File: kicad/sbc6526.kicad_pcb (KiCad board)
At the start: 4 copper layers, 100 x 100 mm, 61 parts, among them P1 2k, P2 5k, SW1 UP, SW2 DOWN, SW3 OK, SW4 CANCEL, SW5 RESET, U1 6526, U10 74AC138, U11 74ACT245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

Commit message: Fixed Freq. Meter footprint
Frequency meter footprint was wrong. Top row was reversed.

Minor additions to bootstrap and firmware.
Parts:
- moved R8 14.7 mm to (119.2, 127.9), turned to 180 degrees
- moved R7 9.73 mm to (107.0, 128.0), turned to 0 degrees
- moved R5 0.58 mm to (111.6, 128.0), turned to 180 degrees
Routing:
- net Net-(PIC1-Pad13): track 58.7 -> 20.0 mm
- net /clockmeter/C1: track 7.94 -> 25.5 mm
- net Net-(PIC1-Pad12): track 21.6 -> 35.2 mm
- net /clockmeter/C3: track 29.0 -> 21.8 mm
- net Net-(PIC1-Pad10): track 49.0 -> 55.8 mm
- net /clockmeter/C2: track 16.6 -> 18.7 mm
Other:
- board text added: "sbc6526 v2.0.1"
- board text removed: "sbc6526 v2.0.0"

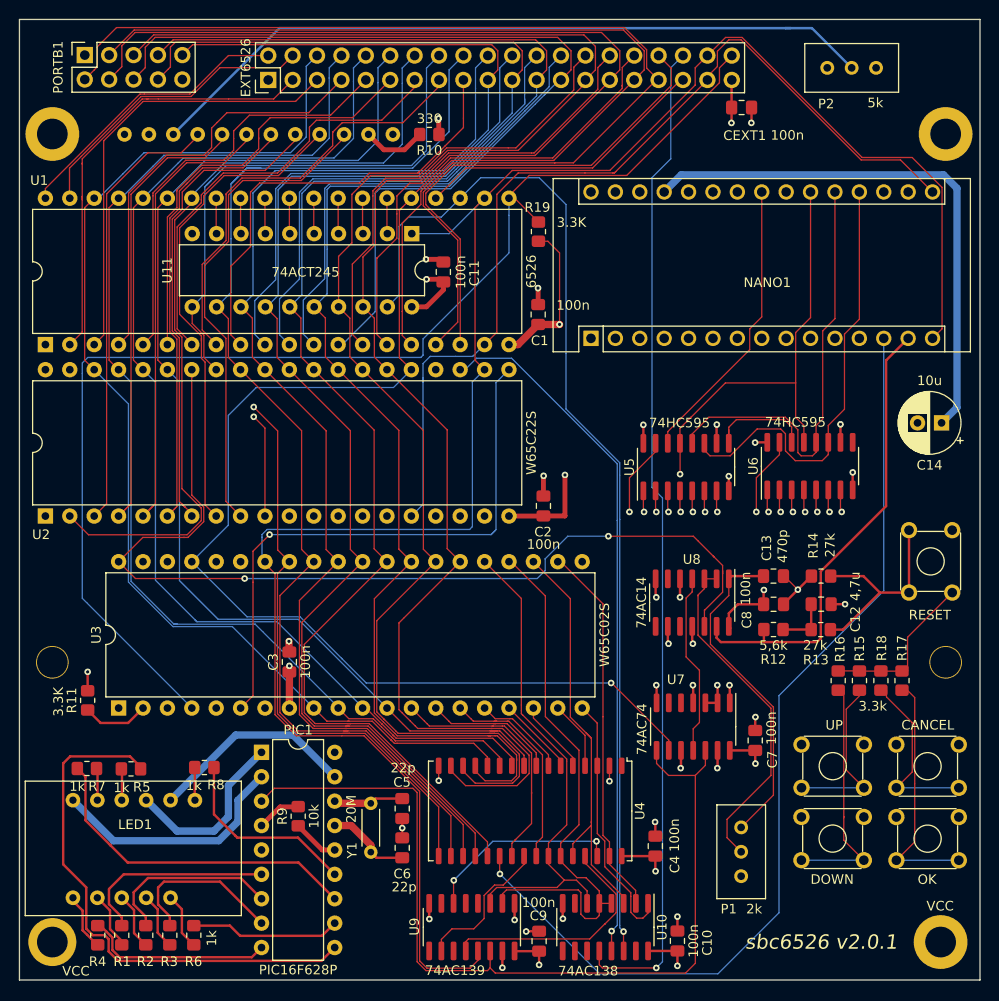
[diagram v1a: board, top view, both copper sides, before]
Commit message: Fixes
* Minor fixes to routing
* Right VCC hole was slightly offset. Fixed
* Removed /CE from arduino to RAM. As RAMCE pulses with PHI, it's not necessary, and we leave /CE tied to GND.
* Fixed RAM footprint, as it was too wide. Improved routing.
* Added current limiting resistor to LCD Contrast
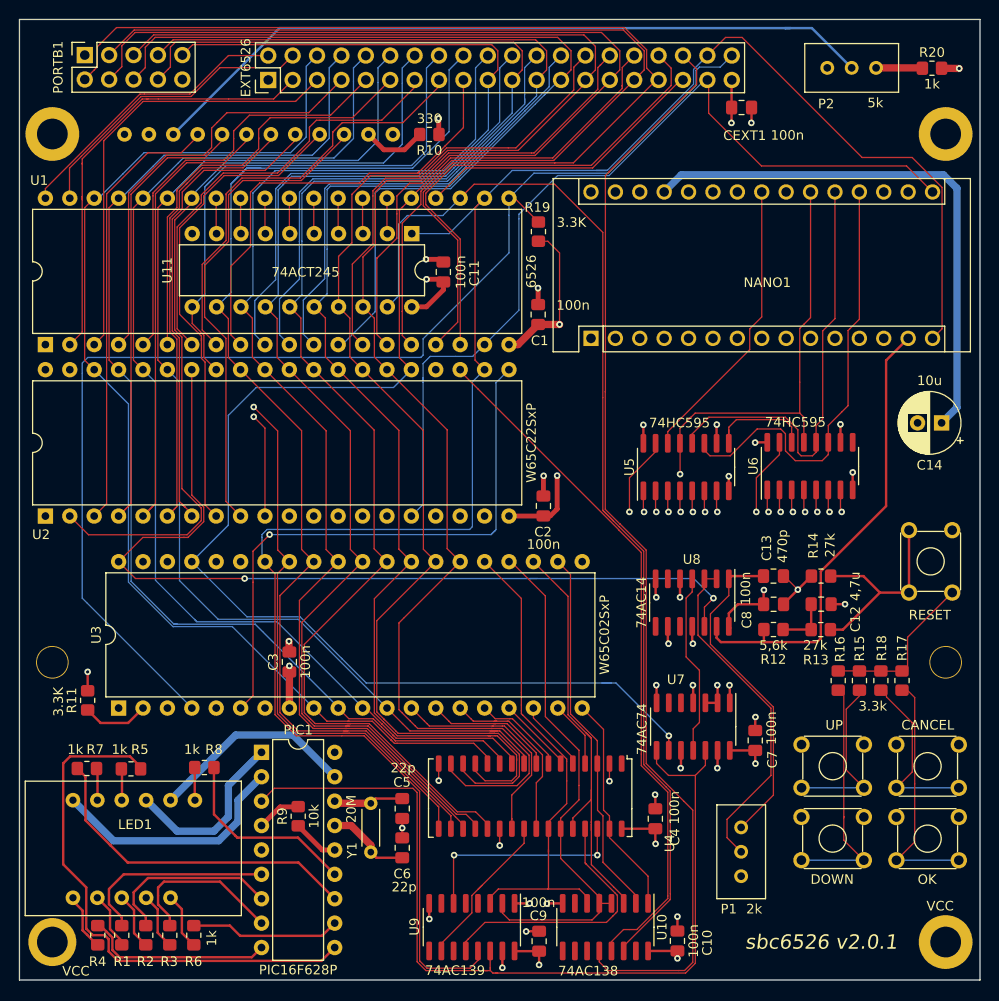
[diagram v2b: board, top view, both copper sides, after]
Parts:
- added R20: 1k, Resistor_SMD:R_0805_2012Metric_Pad1.20x1.40mm_HandSolder, F.Cu at (195.0, 55.1)
- U2: value W65C22S -> W65C22SxP
- U3: value W65C02S -> W65C02SxP
- moved U4 4.56 mm to (155.0, 135.8)
- moved C4 2.85 mm to (166.2, 133.2)
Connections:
- LCD1 pad : GND -> (no net)
- NANO1 pad 13: /~CE -> no_connect_119
- NANO1 pad 17: no_connect_119 -> no_connect_120
- NANO1 pad 18: no_connect_120 -> no_connect_121
- NANO1 pad 2: no_connect_121 -> no_connect_122
- NANO1 pad 22: no_connect_122 -> no_connect_123
- NANO1 pad 24: no_connect_123 -> no_connect_124
- NANO1 pad 25: no_connect_124 -> no_connect_125
- NANO1 pad 28: no_connect_125 -> no_connect_126
- NANO1 pad 3: no_connect_126 -> no_connect_127
- NANO1 pad 30: no_connect_127 -> no_connect_128
- P1 pad 3: no_connect_128 -> no_connect_129
- P2 pad 1: GND -> Net-(P2-Pad1)
- PIC1 pad 18: no_connect_129 -> no_connect_130
- U10 pad 10: no_connect_130 -> no_connect_131
- U10 pad 11: no_connect_131 -> no_connect_132
- U10 pad 15: no_connect_132 -> no_connect_133
- U10 pad 7: no_connect_133 -> no_connect_134
- U10 pad 9: no_connect_134 -> no_connect_135
- U2 pad 15: no_connect_135 -> no_connect_136
- U2 pad 17: no_connect_136 -> no_connect_137
- U2 pad 18: no_connect_137 -> no_connect_138
- U2 pad 19: no_connect_138 -> no_connect_139
- U2 pad 39: no_connect_139 -> no_connect_140
- U2 pad 40: no_connect_140 -> no_connect_141
- U3 pad 1: no_connect_141 -> no_connect_142
- U3 pad 3: no_connect_142 -> no_connect_143
- U3 pad 39: no_connect_143 -> no_connect_144
- U3 pad 5: no_connect_144 -> no_connect_145
- U3 pad 7: no_connect_145 -> no_connect_146
- U4 pad 1: no_connect_146 -> no_connect_147
- U4 pad 22: /~CE -> GND
- U4 pad 3: /A11 -> /A12
- U4 pad 31: /A12 -> /A11
- U6 pad 9: no_connect_147 -> no_connect_148
- U7 pad 5: no_connect_148 -> no_connect_149
- U7 pad 6: no_connect_149 -> no_connect_150
- U8 pad 10: no_connect_150 -> no_connect_151
- U8 pad 6: no_connect_151 -> no_connect_152
- U8 pad 8: no_connect_152 -> no_connect_153
- U9 pad 11: no_connect_153 -> no_connect_154
- U9 pad 4: no_connect_154 -> no_connect_155
- U9 pad 5: no_connect_155 -> no_connect_156
- U9 pad 7: no_connect_156 -> no_connect_157
- U9 pad 9: no_connect_157 -> no_connect_158
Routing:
- net /~CE: track 102.2 -> 0.00 mm, vias 1 -> 0
- net /~CIAEXT: track 104.6 -> 114.3 mm, vias 1 -> 0
- net /~RES: track 102.1 -> 94.6 mm
- net /~CIA: track 109.7 -> 115.4 mm, vias 1 -> 0
- net /TOD: track 100.0 -> 95.1 mm
- net Net-(P2-Pad1): track 0.00 -> 4.84 mm
- net GND: track 48.3 -> 52.0 mm, vias 25 -> 27
- net /A11: track 65.1 -> 61.7 mm
- net /A4: track 65.3 -> 62.2 mm
- net /memory/~WE: track 25.2 -> 28.2 mm
- net /A6: track 57.8 -> 55.0 mm
- net /D1: track 191.6 -> 188.8 mm
- net /D0: track 188.6 -> 185.8 mm
- net /D2: track 181.6 -> 179.4 mm
- net /D3: track 177.0 -> 174.8 mm
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
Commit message: Uploaded firmware v2.0.2
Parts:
- moved R10 1.08 mm to (143.8, 62.0)
- moved U7 0.10 mm to (170.0, 123.6)
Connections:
- net /R~W renamed /R~{W}
- net /memory/~OE renamed /memory/~{OE}
- net /memory/~WE renamed /memory/~{WE}
- net /peripherals/~CIARES renamed /peripherals/~{CIARES}
- net /peripherals/~EXTFLAG renamed /peripherals/~{EXTFLAG}
- net /peripherals/~EXTPC renamed /peripherals/~{EXTPC}
- net /~CIA renamed /~{CIA}
- net /~CIAEXT renamed /~{CIAEXT}
- net /~IRQ renamed /~{IRQ}
- net /~PHI2 renamed /~{PHI2}
- net /~RES renamed /~{RES}
- net /~VIA renamed /~{VIA}
- net /~VIAIRQ renamed /~{VIAIRQ}
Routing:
- net Net-(LCD1-Pad15): track 6.67 -> 7.73 mm
- net /peripherals/PA7: track 47.8 -> 48.6 mm
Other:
- board text added: "sbc6526 v2.0.2"
- board text removed: "sbc6526 v2.0.1"

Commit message: PullUps con SERCLOCK and SERDAT
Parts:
- added R21: 3k3, Resistor_SMD:R_0805_2012Metric_Pad1.20x1.40mm_HandSolder, F.Cu at (102.7, 72.3)
- added R22: 3k3, Resistor_SMD:R_0805_2012Metric_Pad1.20x1.40mm_HandSolder, F.Cu at (105.2, 72.3)
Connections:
- net /BE renamed /bootstrap/BE
- net /PB0 renamed /io/PB0
- net /PB1 renamed /io/PB1
- net /PB2 renamed /io/PB2
- net /PB3 renamed /io/PB3
- net /PB4 renamed /io/PB4
- net /PB5 renamed /io/PB5
- net /PB6 renamed /io/PB6
- net /PB7 renamed /io/PB7
- net /RESET renamed /bootstrap/RESET
- net /VPB1 renamed /peripherals/VPB1
- net /VPB2 renamed /peripherals/VPB2
- net /VPB3 renamed /peripherals/VPB3
- net /VPB4 renamed /peripherals/VPB4
- net /~{CIAEXT} renamed /memory/~{CIAEXT}
- net /~{CIA} renamed /memory/~{CIA}
- net /~{PHI2} renamed /clock/~{PHI2}
- net /~{VIA} renamed /memory/~{VIA}
- LCD1 pad : (no net) -> GND
- NANO1 pad 1: no_connect_118 -> unconnected-(NANO1-Pad1)
- NANO1 pad 13: no_connect_119 -> unconnected-(NANO1-Pad13)
- NANO1 pad 17: no_connect_120 -> unconnected-(NANO1-Pad17)
- NANO1 pad 18: no_connect_121 -> unconnected-(NANO1-Pad18)
- NANO1 pad 2: no_connect_122 -> unconnected-(NANO1-Pad2)
- NANO1 pad 22: no_connect_123 -> unconnected-(NANO1-Pad22)
- NANO1 pad 24: no_connect_124 -> unconnected-(NANO1-Pad24)
- NANO1 pad 25: no_connect_125 -> unconnected-(NANO1-Pad25)
- NANO1 pad 28: no_connect_126 -> unconnected-(NANO1-Pad28)
- NANO1 pad 3: no_connect_127 -> unconnected-(NANO1-Pad3)
- NANO1 pad 30: no_connect_128 -> unconnected-(NANO1-Pad30)
- P1 pad 3: no_connect_129 -> unconnected-(P1-Pad3)
- PIC1 pad 18: no_connect_130 -> unconnected-(PIC1-Pad18)
- U10 pad 10: no_connect_131 -> unconnected-(U10-Pad10)
- U10 pad 11: no_connect_132 -> unconnected-(U10-Pad11)
- U10 pad 15: no_connect_133 -> unconnected-(U10-Pad15)
- U10 pad 7: no_connect_134 -> unconnected-(U10-Pad7)
- U10 pad 9: no_connect_135 -> unconnected-(U10-Pad9)
- U2 pad 15: no_connect_136 -> unconnected-(U2-Pad15)
- U2 pad 17: no_connect_137 -> unconnected-(U2-Pad17)
- U2 pad 18: no_connect_138 -> unconnected-(U2-Pad18)
- U2 pad 19: no_connect_139 -> unconnected-(U2-Pad19)
- U2 pad 39: no_connect_140 -> unconnected-(U2-Pad39)
- U2 pad 40: no_connect_141 -> unconnected-(U2-Pad40)
- U3 pad 1: no_connect_142 -> unconnected-(U3-Pad1)
- U3 pad 3: no_connect_143 -> unconnected-(U3-Pad3)
- U3 pad 35: (no net) -> unconnected-(U3-Pad35)
- U3 pad 39: no_connect_144 -> unconnected-(U3-Pad39)
- U3 pad 5: no_connect_145 -> unconnected-(U3-Pad5)
- U3 pad 7: no_connect_146 -> unconnected-(U3-Pad7)
- U4 pad 1: no_connect_147 -> unconnected-(U4-Pad1)
- U6 pad 9: no_connect_148 -> unconnected-(U6-Pad9)
- U7 pad 5: no_connect_149 -> unconnected-(U7-Pad5)
- U7 pad 6: no_connect_150 -> unconnected-(U7-Pad6)
- U8 pad 10: no_connect_151 -> unconnected-(U8-Pad10)
- U8 pad 6: no_connect_152 -> unconnected-(U8-Pad6)
- U8 pad 8: no_connect_153 -> unconnected-(U8-Pad8)
- U9 pad 11: no_connect_154 -> unconnected-(U9-Pad11)
- U9 pad 4: no_connect_155 -> unconnected-(U9-Pad4)
- U9 pad 5: no_connect_156 -> unconnected-(U9-Pad5)
- U9 pad 7: no_connect_157 -> unconnected-(U9-Pad7)
- U9 pad 9: no_connect_158 -> unconnected-(U9-Pad9)
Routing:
- net /peripherals/SERCLK: track 30.5 -> 33.2 mm
- net /peripherals/SERDAT: track 31.2 -> 33.9 mm
- net /PHI2: track 148.7 -> 146.8 mm
- net Net-(U5-Pad9): track 11.9 -> 10.5 mm
- net /memory/~{OE}: track 17.5 -> 16.3 mm
- net /A14: track 95.0 -> 94.0 mm
- net /A13: track 80.8 -> 79.9 mm
- net /A3: track 160.2 -> 159.4 mm
- net /D0: track 185.8 -> 185.1 mm
- net /D6: track 159.5 -> 158.9 mm
- net Net-(LCD1-Pad3): track 77.5 -> 76.9 mm
- net /A1: track 165.2 -> 164.7 mm
- net /D5: track 162.0 -> 161.5 mm
- net VCC: track 165.6 -> 165.5 mm, vias 21 -> 22
